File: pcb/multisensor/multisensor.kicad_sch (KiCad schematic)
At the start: 25 parts, among them J1 TTL_Serial, J2 mmWave_Data, J3 mmWave_Support, J4 PIR_Sensor, J5 BME680, J6 BH1750, J7 10118193-0001LF, Q1 PN2222A, Q2 PN2222A, SW1 RESET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

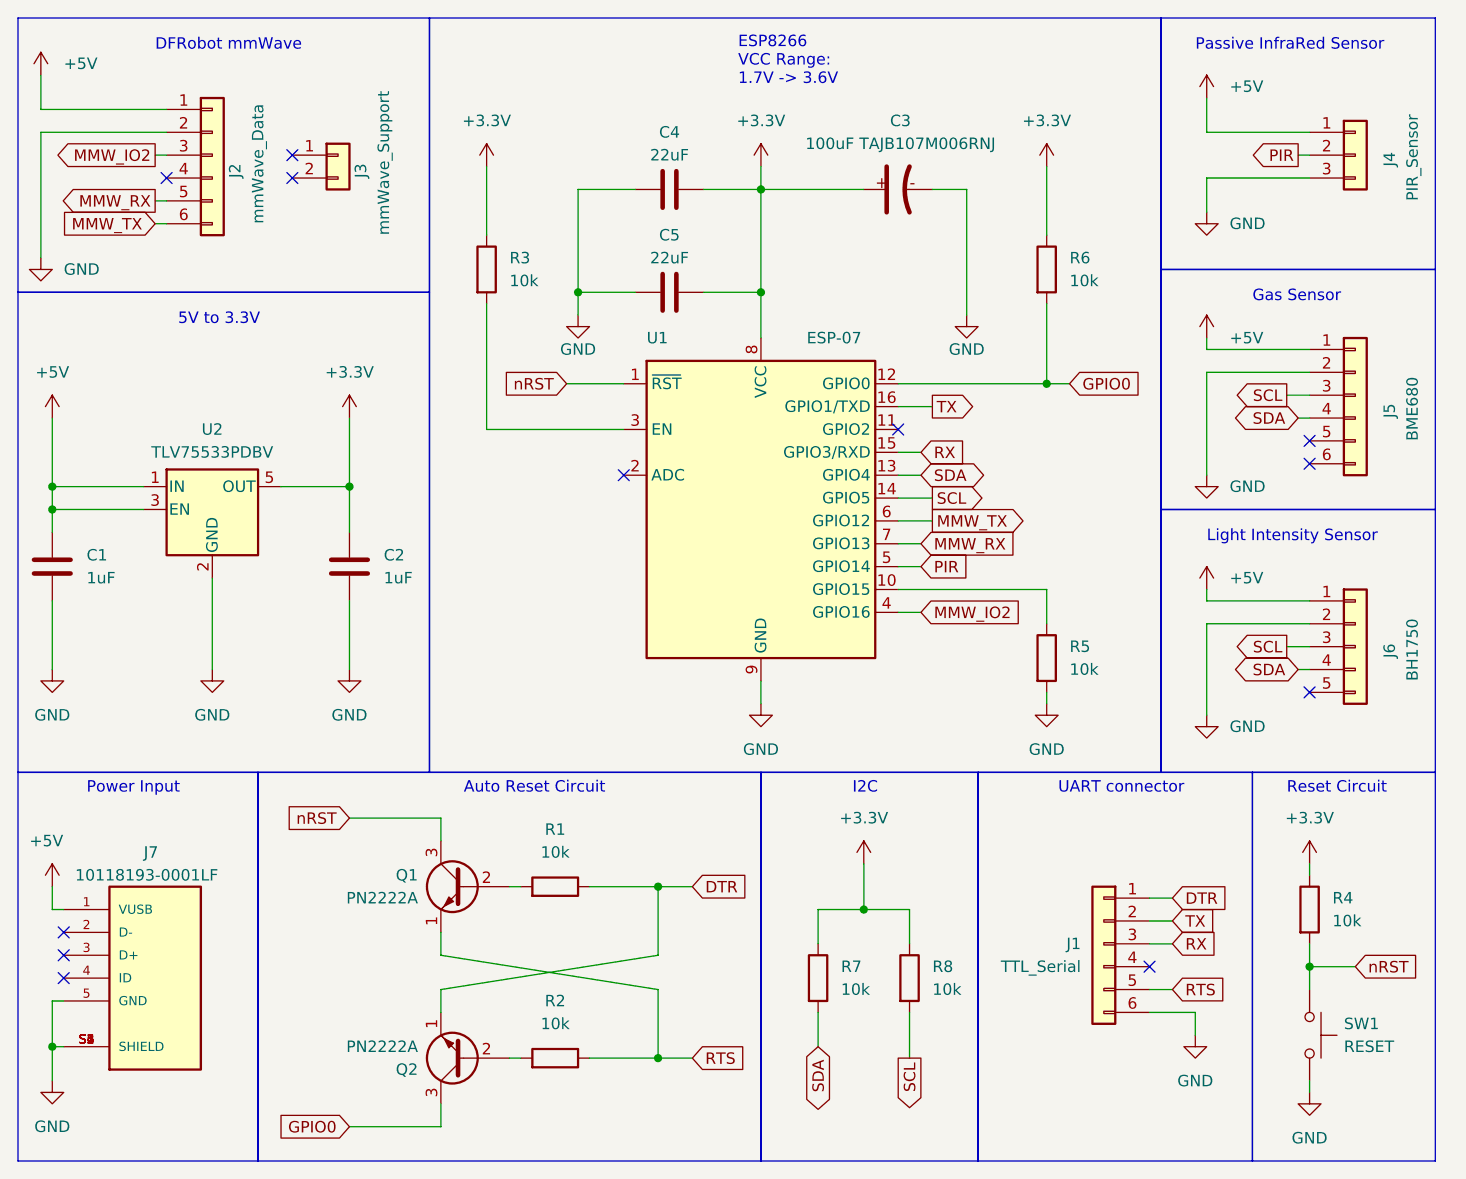
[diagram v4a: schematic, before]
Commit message: add spice simulations and manufacturing files
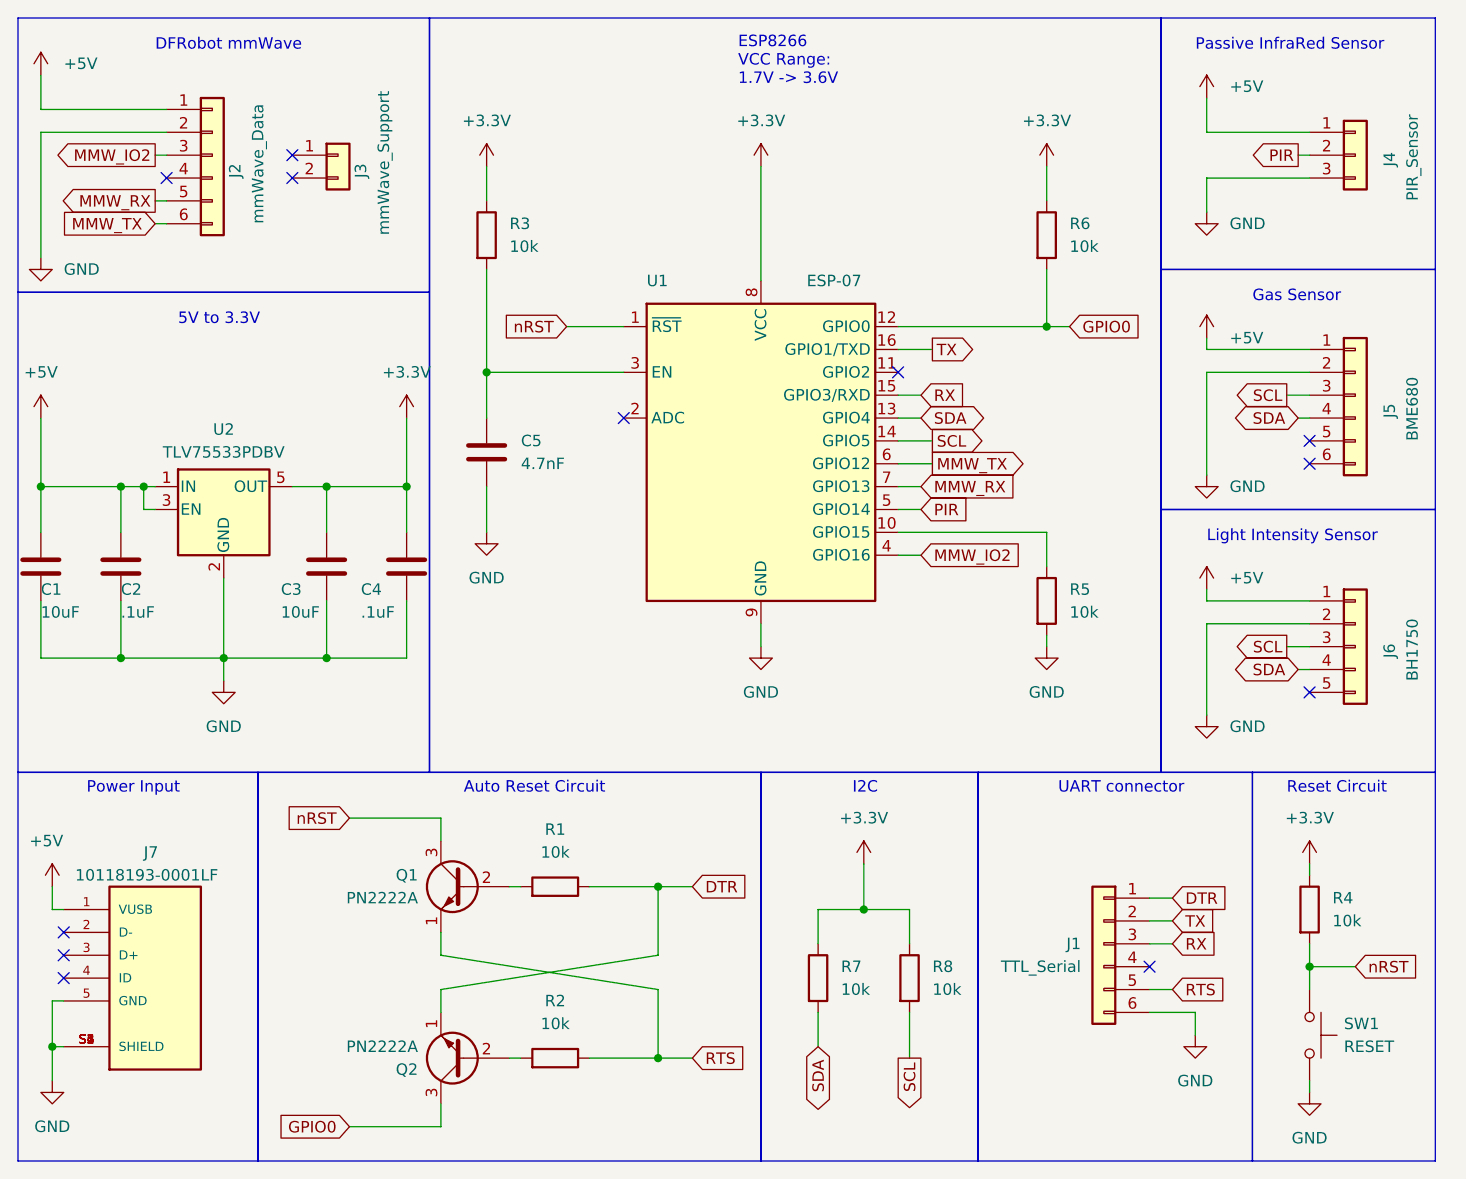
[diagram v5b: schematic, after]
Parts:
- removed C3: 100uF TAJB107M006RNJ, *Multisensor:AVX-B, symbol TAJB107M006RNJ:TANTALUM-SMD-100UF-6.3V_AVX-B_
- added C1: 10uF, Capacitor_SMD:C_1206_3216Metric, symbol Device:C
- C2: renamed from C1; value 1uF -> .1uF; MPN NMC1206X7R105K50TRPLPF -> C1206C104K5RAC7800
- C3: renamed from C2; value 1uF -> 10uF; MPN NMC1206X7R105K50TRPLPF -> CL31B106KAHNNNE
- C4: value 22uF -> .1uF; footprint Capacitor_SMD:C_1210_3225Metric -> Capacitor_SMD:C_1206_3216Metric; MPN CL32A226MOJNNNE -> C1206C104K5RAC7800
- C5: value 22uF -> 4.7nF; footprint Capacitor_SMD:C_1210_3225Metric -> Capacitor_SMD:C_1206_3216Metric; MPN CL32A226MOJNNNE -> KGM31TR72D472KU
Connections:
- net +3.3V: now also C4.1; no longer C4.2, C5.2
- net +5V: now also C1.1
- net GND: now also C4.2, C5.2, C1.2; no longer C4.1, C5.1
- net at R3.2, U1.3 (EN): now also C5.1
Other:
- moved on the sheet: C2, C3, R3, R5, R6, U1, U2

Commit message: update gerber files
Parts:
- J1, J2: MPN (none) -> PPPC061LFBN-RC
- J3: MPN (none) -> PPPC021LFBN-RC
- J4: MPN (none) -> PPPC031LFBN-RC
- J5: MPN (none) -> PPPC061LGBN-RC
- J6: MPN (none) -> PPPC051LGBN-RC
- J7: MP 10118193-0001LF -> (none); MPN (none) -> 10118193-0001LF
- Q1, Q2: MPN (none) -> MMBT2222A-TP
- R1, R2, R3, R4, R5, R6, R7, R8: MPN (none) -> RMCF0805FT10K0
- SW1: MPN (none) -> TS02-66-60-BK-160-LCR-D
- U1: Customer Supply (none) -> DNP; MPN (none) -> ESP-07
- U2: MPN (none) -> TLV75533PDBVR
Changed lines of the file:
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@@
       (effects (font (size 1.27 1.27)) (justify left) hide)
     )
+    (property "MPN" "MMBT2222A-TP" (at 120.65 146.05 0)
+      (effects (font (size 1.27 1.27)) hide)
+    )
     (pin "1")
     (pin "2")
@@
     )
     (property "Datasheet" "~" (at 106.68 45.72 0)
+      (effects (font (size 1.27 1.27)) hide)
+    )
+    (property "MPN" "PPPC021LFBN-RC" (at 106.68 45.72 90)
       (effects (font (size 1.27 1.27)) hide)
     )
@@
       (effects (font (size 1.27 1.27)) (justify left) hide)
     )
+    (property "MPN" "MMBT2222A-TP" (at 120.65 127 0)
+      (effects (font (size 1.27 1.27)) hide)
+    )
     (pin "1")
     (pin "2")
@@
       (effects (font (size 1.27 1.27)) hide)
     )
+    (property "MPN" "RMCF0805FT10K0" (at 130.81 146.05 90)
+      (effects (font (size 1.27 1.27)) hide)
+    )
     (pin "1")
     (pin "2")
@@
       (effects (font (size 1.27 1.27)) hide)
     )
+    (property "MPN" "RMCF0805FT10K0" (at 170.18 137.16 0)
+      (effects (font (size 1.27 1.27)) hide)
+    )
     (pin "1")
     (pin "2")
@@
       (effects (font (size 1.27 1.27)) hide)
     )
+    (property "MPN" "RMCF0805FT10K0" (at 123.19 54.61 0)
+      (effects (font (size 1.27 1.27)) hide)
+    )
     (pin "1")
     (pin "2")
@@
       (effects (font (size 1.27 1.27)) hide)
     )
+    (property "MPN" "PPPC031LFBN-RC" (at 219.71 45.72 90)
+      (effects (font (size 1.27 1.27)) hide)
+    )
     (pin "1")
     (pin "2")
@@
     )
     (property "Datasheet" "~" (at 219.71 143.51 0)
+      (effects (font (size 1.27 1.27)) hide)
+    )
+    (property "MPN" "TS02-66-60-BK-160-LCR-D" (at 214.63 143.51 90)
       (effects (font (size 1.27 1.27)) hide)
     )
@@
       (effects (font (size 1.27 1.27)) (justify bottom) hide)
     )
-    (property "MP" "10118193-0001LF" (at 86.36 137.16 0)
+    (property "MPN" "10118193-0001LF" (at 86.36 137.16 0)
       (effects (font (size 1.27 1.27)) (justify bottom) hide)
     )
@@
       (effects (font (size 1.27 1.27)) hide)
     )
+    (property "MPN" "PPPC061LFBN-RC" (at 92.71 45.72 90)
+      (effects (font (size 1.27 1.27)) hide)
+    )
     (pin "1")
     (pin "2")
@@
       (effects (font (size 1.27 1.27)) hide)
     )
+    (property "MPN" "RMCF0805FT10K0" (at 130.81 127 90)
+      (effects (font (size 1.27 1.27)) hide)
+    )
     (pin "1")
     (pin "2")
@@
     )
     (property "Datasheet" "https://docs.ai-thinker.com/_media/esp8266/esp8266_series_modules_user_manual_en.pdf" (at 144.78 77.47 0)
+      (effects (font (size 1.27 1.27)) hide)
+    )
+    (property "MPN" "ESP-07" (at 153.67 80.01 0)
+      (effects (font (size 1.27 1.27)) hide)
+    )
+    (property "Customer Supply" "DNP" (at 153.67 80.01 0)
+      (effects (font (size 1.27 1.27)) hide)
+    )
+    (property "Customer Remark" "" (at 153.67 80.01 0)
       (effects (font (size 1.27 1.27)) hide)
     )
@@
       (effects (font (size 1.27 1.27)) hide)
     )
+    (property "MPN" "PPPC061LGBN-RC" (at 219.71 72.39 90)
+      (effects (font (size 1.27 1.27)) hide)
+    )
     (pin "1")
     (pin "2")
@@
       (effects (font (size 1.27 1.27)) hide)
     )
+    (property "MPN" "RMCF0805FT10K0" (at 185.42 54.61 0)
+      (effects (font (size 1.27 1.27)) hide)
+    )
     (pin "1")
     (pin "2")
@@
     )
     (property "Datasheet" "~" (at 219.71 100.33 0)
+      (effects (font (size 1.27 1.27)) hide)
+    )
+    (property "MPN" "PPPC051LGBN-RC" (at 219.71 100.33 90)
       (effects (font (size 1.27 1.27)) hide)
     )
@@
     )
     (property "Datasheet" "~" (at 191.77 133.35 0)
+      (effects (font (size 1.27 1.27)) hide)
+    )
+    (property "MPN" "PPPC061LFBN-RC" (at 191.77 133.35 0)
       (effects (font (size 1.27 1.27)) hide)
     )
@@
       (effects (font (size 1.27 1.27)) hide)
     )
+    (property "MPN" "RMCF0805FT10K0" (at 214.63 129.54 0)
+      (effects (font (size 1.27 1.27)) hide)
+    )
     (pin "1")
     (pin "2")
@@
     )
     (property "Datasheet" "~" (at 185.42 95.25 0)
+      (effects (font (size 1.27 1.27)) hide)
+    )
+    (property "MPN" "RMCF0805FT10K0" (at 185.42 95.25 0)
       (effects (font (size 1.27 1.27)) hide)
     )
@@
     )
     (property "Sim.Library" "../3rdparty/spice/TLV75533P_TRANS.lib" (at 93.98 85.09 0)
+      (effects (font (size 1.27 1.27)) hide)
+    )
+    (property "MPN" "TLV75533PDBVR" (at 93.98 85.09 0)
       (effects (font (size 1.27 1.27)) hide)
     )
@@
       (effects (font (size 1.27 1.27)) hide)
     )
+    (property "MPN" "RMCF0805FT10K0" (at 160.02 137.16 0)
+      (effects (font (size 1.27 1.27)) hide)
+    )

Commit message: fix pcb layout
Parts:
- removed Q1, Q2: PN2222A, Package_TO_SOT_SMD:SOT-23, symbol Transistor_BJT:PN2222A
- added Q1, Q2: PN2222A, Package_TO_SOT_SMD:SOT-23, symbol Transistor_BJT:MMBT3904
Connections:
- net DTR: now also Q2.2 (E)
- net GPIO0: now also Q2.3 (C)
- net RTS: now also Q1.2 (E)
- net nRST: now also Q1.3 (C)
- net at R2.2: now also Q2.1 (B)
- net at R1.2: now also Q1.1 (B)
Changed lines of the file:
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@@
-    )
-  )
-  (symbol (lib_id "Transistor_BJT:PN2222A") (at 120.65 146.05 180) (unit 1)
-    (in_bom yes) (on_board yes) (dnp no)
-    (property "Reference" "Q2" (at 115.57 147.32 0)
-      (effects (font (size 1.27 1.27)) (justify left))
-    )
-    (property "Value" "PN2222A" (at 115.57 144.78 0)
-      (effects (font (size 1.27 1.27)) (justify left))
-    )
-    (property "Footprint" "Package_TO_SOT_SMD:SOT-23" (at 115.57 144.145 0)
-      (effects (font (size 1.27 1.27) italic) (justify left) hide)
-    )
-    (property "Datasheet" "https://www.onsemi.com/pub/Collateral/PN2222-D.PDF" (at 120.65 146.05 0)
-      (effects (font (size 1.27 1.27)) (justify left) hide)
-    )
-    (property "MPN" "MMBT2222A-TP" (at 120.65 146.05 0)
-      (effects (font (size 1.27 1.27)) hide)
-    )
-    (pin "1")
-    (pin "2")
-    (pin "3")
-    (instances
-      (project "multisensor"
-        (path "/e8407b76-28a5-49b8-a72f-f5bc1cfd4075"
-          (reference "Q2") (unit 1)
-        )
-      )
     )
   )
@@
         (path "/e8407b76-28a5-49b8-a72f-f5bc1cfd4075"
           (reference "J3") (unit 1)
-        )
-      )
-    )
-  )
-  (symbol (lib_id "Transistor_BJT:PN2222A") (at 120.65 127 0) (mirror y) (unit 1)
-    (in_bom yes) (on_board yes) (dnp no) (fields_autoplaced)
-    (property "Reference" "Q1" (at 115.57 125.73 0)
-      (effects (font (size 1.27 1.27)) (justify left))
-    )
-    (property "Value" "PN2222A" (at 115.57 128.27 0)
-      (effects (font (size 1.27 1.27)) (justify left))
-    )
-    (property "Footprint" "Package_TO_SOT_SMD:SOT-23" (at 115.57 128.905 0)
-      (effects (font (size 1.27 1.27) italic) (justify left) hide)
-    )
-    (property "Datasheet" "https://www.onsemi.com/pub/Collateral/PN2222-D.PDF" (at 120.65 127 0)
-      (effects (font (size 1.27 1.27)) (justify left) hide)
-    )
-    (property "MPN" "MMBT2222A-TP" (at 120.65 127 0)
-      (effects (font (size 1.27 1.27)) hide)
-    )
-    (pin "1")
-    (pin "2")
-    (pin "3")
-    (instances
-      (project "multisensor"
-        (path "/e8407b76-28a5-49b8-a72f-f5bc1cfd4075"
-          (reference "Q1") (unit 1)
         )
       )
@@
     )
   )
+  (symbol (lib_id "Transistor_BJT:MMBT3904") (at 120.65 127 0) (mirror y) (unit 1)
+    (in_bom yes) (on_board yes) (dnp no)
+    (property "Reference" "Q1" (at 115.57 125.73 0)
+      (effects (font (size 1.27 1.27)) (justify left))
+    )
+    (property "Value" "PN2222A" (at 115.57 128.27 0)
+      (effects (font (size 1.27 1.27)) (justify left))
+    )
+    (property "Footprint" "Package_TO_SOT_SMD:SOT-23" (at 115.57 128.905 0)
+      (effects (font (size 1.27 1.27) italic) (justify left) hide)
+    )
+    (property "Datasheet" "https://www.mccsemi.com/pdf/Products/MMBT2222A(SOT-23).pdf" (at 120.65 127 0)
+      (effects (font (size 1.27 1.27)) (justify left) hide)
+    )
+    (property "MPN" "MMBT2222A-TP" (at 120.65 127 0)
+      (effects (font (size 1.27 1.27)) hide)
+    )
+    (pin "1")
+    (pin "2")
+    (pin "3")
+    (instances
+      (project "multisensor"
+        (path "/e8407b76-28a5-49b8-a72f-f5bc1cfd4075"
+          (reference "Q1") (unit 1)
+        )
+      )
+    )
+  )
   (symbol (lib_id "power:GND") (at 185.42 100.33 0) (unit 1)
     (in_bom yes) (on_board yes) (dnp no) (fields_autoplaced)
@@
         )
       )
+    )
+  )
+  (symbol (lib_id "Transistor_BJT:MMBT3904") (at 120.65 146.05 180) (unit 1)
+    (in_bom yes) (on_board yes) (dnp no) (fields_autoplaced)
+    (property "Reference" "Q2" (at 115.57 144.78 0)
+      (effects (font (size 1.27 1.27)) (justify left))
+    )
+    (property "Value" "PN2222A" (at 115.57 147.32 0)
+      (effects (font (size 1.27 1.27)) (justify left))
+    )
+    (property "Footprint" "Package_TO_SOT_SMD:SOT-23" (at 115.57 144.145 0)
+      (effects (font (size 1.27 1.27) italic) (justify left) hide)
+    )
+    (property "Datasheet" "https://www.onsemi.com/pdf/datasheet/pzt3904-d.pdf" (at 120.65 146.05 0)
+      (effects (font (size 1.27 1.27)) (justify left) hide)
+    )
+    (property "MPN" "MMBT2222A-TP" (at 120.65 146.05 0)
+      (effects (font (size 1.27 1.27)) hide)
+    )
+    (pin "1")
+    (pin "2")
+    (pin "3")
+    (instances
+      (project "multisensor"
+        (path "/e8407b76-28a5-49b8-a72f-f5bc1cfd4075"
+          (reference "Q2") (unit 1)
+        )
+      )
